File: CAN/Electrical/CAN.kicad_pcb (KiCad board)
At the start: 4 copper layers, 26 x 30 mm, 31 parts, among them J1 Conn_01x04, P1 USB_C_Plug_USB2.0, Q1 BSS214NW, Q2 BSS214NW, SW1 SW_Push, SW2 SW_DIP_x02, U1 ESP32-C3-MINI-1, U2 AP2112K-3.3, U3 SN65HVD230

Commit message: Updated project
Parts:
- TP5: value TestPoint -> VBUS
- TP6: value TestPoint -> 3.3V
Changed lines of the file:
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@@
     (property "ki_keywords" "switch normally-open pushbutton push-button")
     (attr smd)
-    (fp_text reference "SW1" (at 0 -0.254) (layer "F.SilkS")
+    (fp_text reference "SW1" (at -0.508 0) (layer "F.SilkS")
         (effects (font (size 0.5 0.5) (thickness 0.1) bold))
     )
@@
         (effects (font (size 0.8 0.8) (thickness 0.125)) (justify mirror))
     )
-    (fp_text value "TestPoint" (at -2.794 -0.508) (layer "B.SilkS")
+    (fp_text value "3.3V" (at -2.794 -0.508) (layer "B.SilkS")
         (effects (font (size 0.8 0.8) (thickness 0.125)) (justify mirror))
     )
@@
         (effects (font (size 0.8 0.8) (thickness 0.125)) (justify mirror))
     )
-    (fp_text value "TestPoint" (at -3.048 -0.508) (layer "B.SilkS")
+    (fp_text value "VBUS" (at -3.048 -0.508) (layer "B.SilkS")
         (effects (font (size 0.8 0.8) (thickness 0.125)) (justify mirror))
     )
@@
   (segment (start 71.46 89.254) (end 71.81 89.254) (width 0.125) (layer "F.Cu") (net 1))
   (segment (start 76.53 95.649) (end 76.53 99.599) (width 0.125) (layer "F.Cu") (net 1))
+  (segment (start 87.2451 95.504) (end 87.2451 93.4974) (width 0.125) (layer "F.Cu") (net 1))
   (segment (start 66.724 115.316) (end 68.9676 115.316) (width 0.125) (layer "F.Cu") (net 1))
   (segment (start 64.516 89.4936) (end 67.2089 92.1865) (width 0.125) (layer "F.Cu") (net 1))
@@
   (segment (start 71.49675 116.1985) (end 72.8275 114.86775) (width 0.125) (layer "F.Cu") (net 1))
   (segment (start 68.9676 115.316) (end 68.9676 113.0936) (width 0.125) (layer "F.Cu") (net 1))
+  (segment (start 87.2451 93.4974) (end 87.2705 93.472) (width 0.125) (layer "F.Cu") (net 1))
   (segment (start 70.58 102.164) (end 70.58 102.574) (width 0.125) (layer "F.Cu") (net 1))
   (segment (start 77.98 88.414) (end 77.98 88.679) (width 0.125) (layer "F.Cu") (net 1))
   (segment (start 66.675 93.135637) (end 67.624137 92.1865) (width 0.125) (layer "F.Cu") (net 1))
   (segment (start 82.22 88.664) (end 82.22 92.414) (width 0.125) (layer "F.Cu") (net 1))
+  (segment (start 87.2451 97.536) (end 87.2451 95.504) (width 0.125) (layer "F.Cu") (net 1))
   (segment (start 82.48 102.574) (end 82.48 105.49) (width 0.125) (layer "F.Cu") (net 1))
   (segment (start 79.793 108.177) (end 81.77 106.2) (width 0.125) (layer "F.Cu") (net 1))
@@
   (segment (start 70.63 94.424) (end 70.63 92.724) (width 0.125) (layer "F.Cu") (net 1))
   (segment (start 69.58 87.374) (end 71.46 89.254) (width 0.125) (layer "F.Cu") (net 1))
-  (segment (start 87.2451 97.536) (end 87.2451 91.4654) (width 0.125) (layer "F.Cu") (net 1))
   (segment (start 72.8275 110.906982) (end 75.557482 108.177) (width 0.125) (layer "F.Cu") (net 1))
   (segment (start 68.9676 115.316) (end 69.8501 116.1985) (width 0.125) (layer "F.Cu") (net 1))
@@
   (segment (start 87.2451 91.4654) (end 87.2705 91.44) (width 0.125) (layer "F.Cu") (net 1))
   (segment (start 68.796 112.922) (end 68.796 110.032) (width 0.125) (layer "F.Cu") (net 1))
+  (segment (start 87.2705 93.472) (end 87.2705 91.44) (width 0.125) (layer "F.Cu") (net 1))
   (segment (start 71.68 92.674) (end 71.73 92.724) (width 0.125) (layer "F.Cu") (net 1))
   (segment (start 78.505 99.599) (end 78.505 95.649) (width 0.125) (layer "F.Cu") (net 1))
@@
   (segment (start 83.82 87.39) (end 83.82 89.318518) (width 0.125) (layer "B.Cu") (net 2))
   (segment (start 83.82 102.186998) (end 84.836575 102.186998) (width 0.125) (layer "B.Cu") (net 2))
-  (segment (start 86.369417 86.7275) (end 84.738 86.7275) (width 0.125) (layer "B.Cu") (net 2))
   (segment (start 68.1629 91.2605) (end 66.8274 89.925) (width 0.125) (layer "B.Cu") (net 2))
-  (segment (start 83.82 102.186998) (end 85.813002 102.186998) (width 0.125) (layer "B.Cu") (net 2))
-  (segment (start 84.0755 87.39) (end 83.82 87.39) (width 0.125) (layer "B.Cu") (net 2))
-  (segment (start 84.738 86.7275) (end 84.0755 87.39) (width 0.125) (layer "B.Cu") (net 2))
+  (segment (start 86.369417 86.7275) (end 84.4825 86.7275) (width 0.125) (layer "B.Cu") (net 2))
+  (segment (start 86.6775 87.035583) (end 86.369417 86.7275) (width 0.125) (layer "B.Cu") (net 2))
   (segment (start 71.803002 102.186998) (end 83.82 102.186998) (width 0.125) (layer "B.Cu") (net 2))
   (segment (start 87.8965 113.7795) (end 86.614 115.062) (width 0.125) (layer "B.Cu") (net 2))
   (segment (start 83.82 89.318518) (end 81.878018 91.2605) (width 0.125) (layer "B.Cu") (net 2))
+  (segment (start 83.82 102.186998) (end 85.813002 102.186998) (width 0.125) (layer "B.Cu") (net 2))
+  (segment (start 86.6775 87.63128) (end 86.6775 87.035583) (width 0.125) (layer "B.Cu") (net 2))
   (segment (start 64.262 109.728) (end 71.803002 102.186998) (width 0.125) (layer "B.Cu") (net 2))
-  (segment (start 86.7575 101.2425) (end 86.7575 87.115583) (width 0.125) (layer "B.Cu") (net 2))
   (segment (start 81.878018 91.2605) (end 68.1629 91.2605) (width 0.125) (layer "B.Cu") (net 2))
   (segment (start 64.262 110.998) (end 64.262 109.728) (width 0.125) (layer "B.Cu") (net 2))
   (segment (start 84.836575 102.186998) (end 87.8965 105.246923) (width 0.125) (layer "B.Cu") (net 2))
+  (segment (start 86.106 88.20278) (end 86.6775 87.63128) (width 0.125) (layer "B.Cu") (net 2))
   (segment (start 87.8965 105.246923) (end 87.8965 113.7795) (width 0.125) (layer "B.Cu") (net 2))
-  (segment (start 85.813002 102.186998) (end 86.7575 101.2425) (width 0.125) (layer "B.Cu") (net 2))
-  (segment (start 86.7575 87.115583) (end 86.369417 86.7275) (width 0.125) (layer "B.Cu") (net 2))
+  (segment (start 85.813002 102.186998) (end 86.106 101.894) (width 0.125) (layer "B.Cu") (net 2))
+  (segment (start 84.4825 86.7275) (end 83.82 87.39) (width 0.125) (layer "B.Cu") (net 2))
+  (segment (start 86.106 101.894) (end 86.106 88.20278) (width 0.125) (layer "B.Cu") (net 2))
   (segment (start 70.559 90.043) (end 73.476 90.043) (width 0.125) (layer "F.Cu") (net 3))
   (segment (start 73.476 90.043) (end 74.48 89.039) (width 0.125) (layer "F.Cu") (net 3))
@@
   (segment (start 70.7992 107.5944) (end 75.2956 107.5944) (width 0.125) (layer "F.Cu") (net 15))
   (segment (start 70.812 109.366) (end 70.812 107.6072) (width 0.125) (layer "F.Cu") (net 15))
+  (segment (start 85.09 99.584) (end 85.09 97.6161) (width 0.125) (layer "F.Cu") (net 16))
   (segment (start 86.94 90.3385) (end 86.233 91.0455) (width 0.125) (layer "F.Cu") (net 16))
   (segment (start 85.1955 93.472) (end 86.233 92.4345) (width 0.125) (layer "F.Cu") (net 16))
+  (segment (start 85.1701 93.4974) (end 85.1955 93.472) (width 0.125) (layer "F.Cu") (net 16))
   (segment (start 86.233 92.4345) (end 86.233 91.0455) (width 0.125) (layer "F.Cu") (net 16))
   (segment (start 86.94 88.235) (end 86.94 90.3385) (width 0.125) (layer "F.Cu") (net 16))
-  (segment (start 85.1955 93.472) (end 85.1955 99.4785) (width 0.125) (layer "F.Cu") (net 16))
   (segment (start 85.1955 99.4785) (end 85.09 99.584) (width 0.125) (layer "F.Cu") (net 16))
+  (segment (start 85.1701 95.504) (end 85.1701 93.4974) (width 0.125) (layer "F.Cu") (net 16))
   (segment (start 86.095 87.39) (end 86.94 88.235) (width 0.125) (layer "F.Cu") (net 16))
+  (segment (start 85.1701 97.536) (end 85.1701 95.504) (width 0.125) (layer "F.Cu") (net 16))
   (segment (start 71.856 95.224) (end 70.63 95.224) (width 0.125) (layer "F.Cu") (net 16))
   (segment (start 72.35911 95.72711) (end 71.856 95.224) (width 0.125) (layer "F.Cu") (net 16))
+  (segment (start 85.09 97.6161) (end 85.1701 97.536) (width 0.125) (layer "F.Cu") (net 16))
   (segment (start 72.35911 97.75911) (end 72.35911 95.72711) (width 0.125) (layer "F.Cu") (net 16))
   (via (at 65.405 93.424) (size 0.8) (drill 0.4) (layers "F.Cu" "B.Cu") (net 16))

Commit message: Updated board
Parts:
- removed Q1, Q2: BSS214NW, Package_TO_SOT_SMD:SOT-323_SC-70
- removed the R4 at (69.8, 107.6)
- removed SW2: SW_DIP_x02, Button_Switch_SMD:SW_DIP_SPSTx02_Slide_Copal_CHS-02A_W5.08mm_P1.27mm_JPin
- added D2: LED, LED_SMD:LED_0805_2012Metric_Pad1.15x1.40mm_HandSolder, F.Cu at (63.2, 114.2)
- added R3: 5.1k, Resistor_SMD:R_0805_2012Metric_Pad1.20x1.40mm_HandSolder, B.Cu at (64.4, 91.9)
- added R6: 10k, Resistor_SMD:R_0805_2012Metric_Pad1.20x1.40mm_HandSolder, F.Cu at (85.3, 110.1)
- added R7: 120R, Resistor_SMD:R_0805_2012Metric_Pad1.20x1.40mm_HandSolder, F.Cu at (65.5, 101.5)
- added U5: FODM217D, Package_SO:SOP-4_4.4x2.6mm_P1.27mm, F.Cu at (67.6, 112.0)
- D1: value D -> D_Schottky
- J1: value Conn_01x04 -> Conn_01x05; footprint Connector_PinSocket_2.54mm:PinSocket_1x04_P2.54mm_Horizontal -> Connector_PinSocket_2.54mm:PinSocket_1x05_P2.54mm_Horizontal
- R5: value 60R -> 5.1k
- SW1: value SW_Push -> Reset
- moved SW1 21.3 mm to (85.9, 114.8)
- moved C5 20.8 mm to (85.3, 112.1), turned to 0 degrees
- moved TP6 19.2 mm to (63.6, 95.6)
- moved TP8 18.0 mm to (81.2, 94.2)
- moved TP7 18.0 mm to (78.5, 94.2)
- moved TP5 12.7 mm to (63.6, 98.3)
- moved R5 8.36 mm to (63.2, 110.3), turned to -90 degrees
- moved J1 2.80 mm to (71.4, 106.2)
- moved R4 1.80 mm to (63.5, 101.5), turned to -90 degrees
- renumbered R3 to R4
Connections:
- J1 pad 1: Net-(J1-Pin_1) -> /GPIO6
- J1 pad 2: CAN_H -> VBUS
- J1 pad 3: CAN_L -> CAN_H
- J1 pad 4: GND -> CAN_L
- P1 pad B5: unconnected-(P1-VCONN-PadB5) -> Net-(P1-VCONN)
- R5 pad 1: CAN_L -> VBUS
- R5 pad 2: GND -> Net-(D2-A)
- U1 pad 20: unconnected-(U1-GPIO6-Pad20) -> /GPIO6
- U3 pad 8: unconnected-(U3-Rs-Pad8) -> Net-(U3-Rs)
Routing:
- net VBUS: track 89.3 -> 64.4 mm
- net Net-(U3-Rs): track 0.00 -> 24.4 mm, vias 0 -> 2
- net GND: track 148.4 -> 125.1 mm, vias 2 -> 4
- net +3.3V: track 71.8 -> 52.9 mm
- net Net-(R7-Pad2): track 0.00 -> 14.4 mm, vias 0 -> 2
- net Net-(J1-Pin_1): track 14.0 -> 0.00 mm, vias 1 -> 0
- net Net-(P1-VCONN): track 0.00 -> 13.7 mm, vias 0 -> 2
- net CAN_L: track 33.4 -> 21.3 mm
- net /TXD: track 18.1 -> 6.14 mm, vias 2 -> 1
- net CAN_H: track 19.2 -> 30.7 mm, vias 0 -> 1
- net /RXD: track 16.5 -> 5.08 mm, vias 2 -> 1
- net /GPIO6: track 0.00 -> 9.05 mm, vias 0 -> 1
- net /EN: track 37.5 -> 33.7 mm
- net Net-(D1-A): track 18.7 -> 20.7 mm, vias 2 -> 3
- net Net-(D2-A): track 0.00 -> 1.79 mm
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
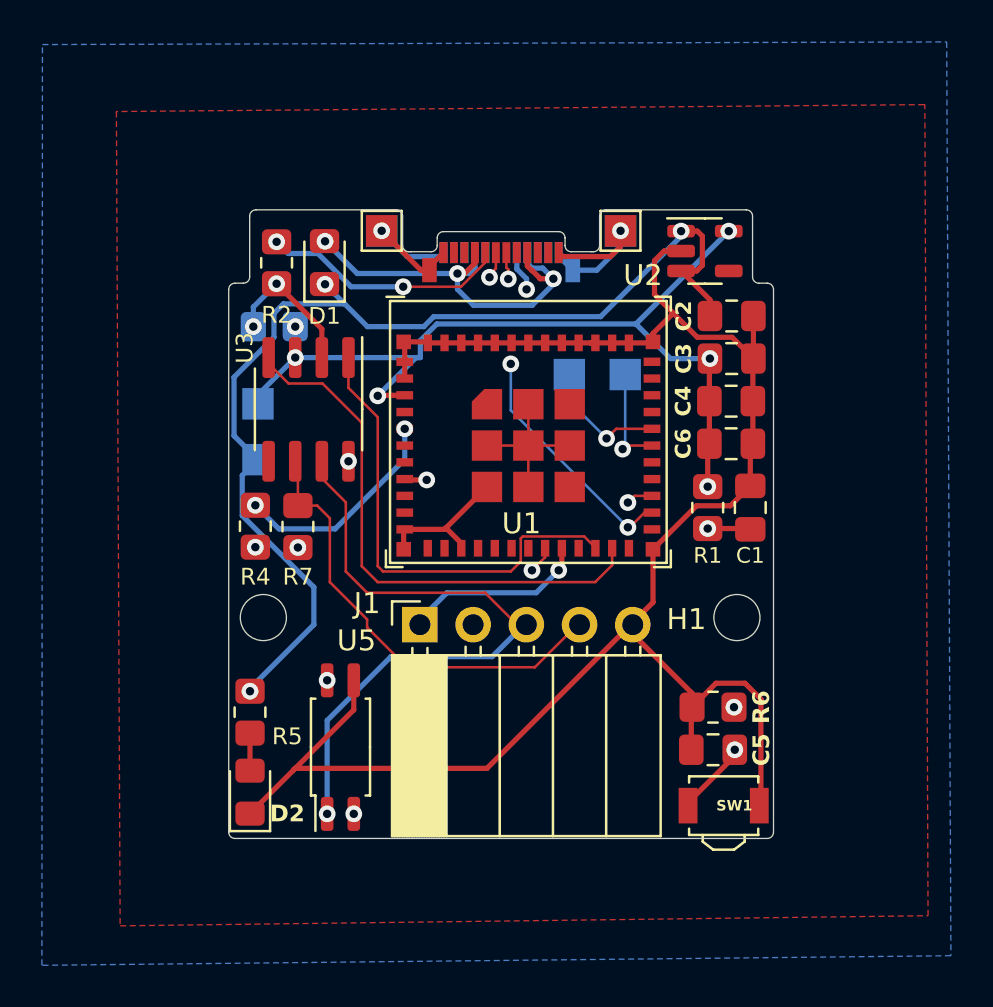
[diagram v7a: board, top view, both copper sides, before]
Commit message: Added Resistor to protect optocoppler diode
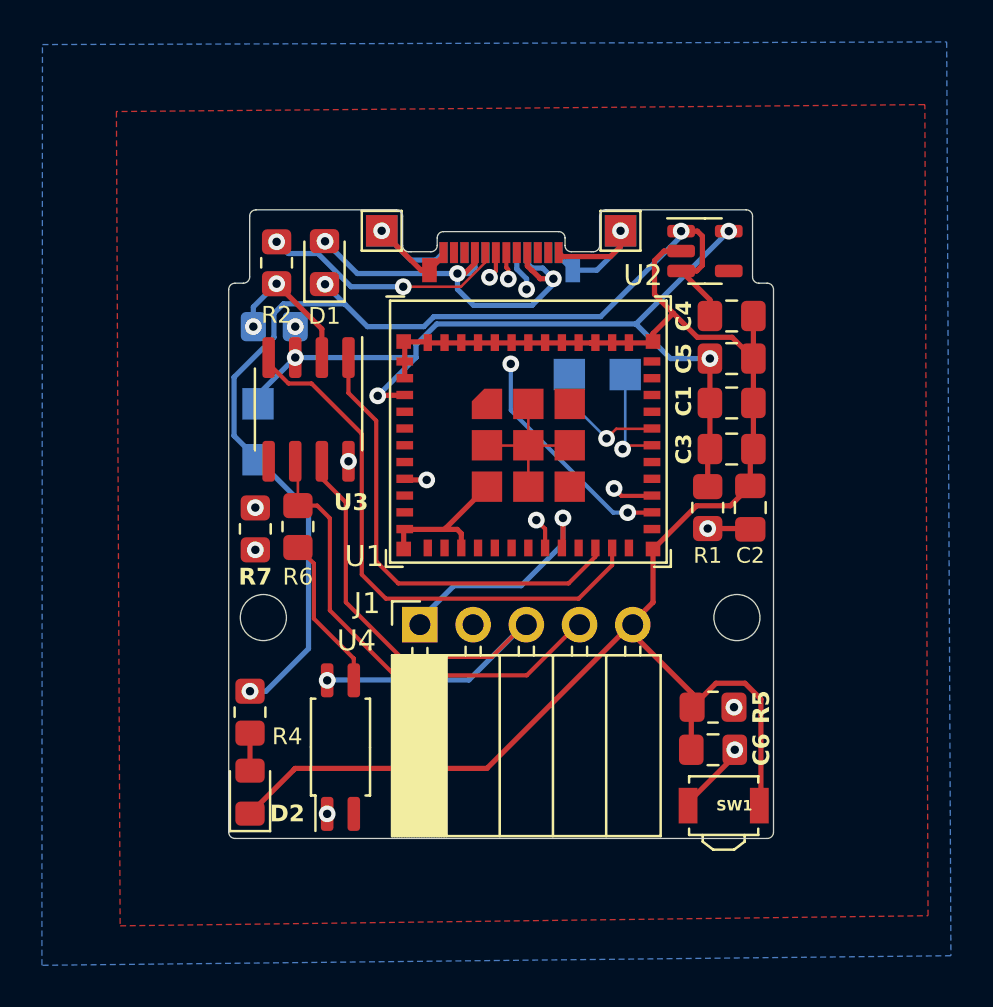
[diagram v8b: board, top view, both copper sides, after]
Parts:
- removed the C4 at (86.2, 95.5)
- removed the C6 at (86.2, 97.5)
- removed the R4 at (63.5, 101.5)
- added C1: 10uF, Capacitor_SMD:C_0805_2012Metric_Pad1.18x1.45mm_HandSolder, F.Cu at (86.2, 95.6)
- added C3: 0.1uF, Capacitor_SMD:C_0805_2012Metric_Pad1.18x1.45mm_HandSolder, F.Cu at (86.2, 97.8)
- added R7: 20R, Resistor_SMD:R_0805_2012Metric_Pad1.20x1.40mm_HandSolder, F.Cu at (63.5, 101.6)
- renumbered C1 to C2, C2 to C4, C3 to C5, C5 to C6, R5 to R4, R6 to R5, R7 to R6, U5 to U4
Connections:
- R6 pad 2: Net-(R7-Pad2) -> Net-(R6-Pad2)
- U1 pad 5: Net-(U1-GPIO2/ADC1_CH2) -> unconnected-(U1-GPIO2/ADC1_CH2-Pad5)
- U4 pad 1: CAN_H -> Net-(R7-Pad2)
- U4 pad 2: Net-(R7-Pad2) -> GND
- U4 pad 3: GND -> Net-(R6-Pad2)
- U4 pad 4: /TERM -> CAN_H
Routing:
- net +3.3V: track 52.9 -> 40.9 mm, vias 6 -> 4
- net Net-(U1-GPIO2/ADC1_CH2): track 10.4 -> 0.00 mm, vias 2 -> 0
- net Net-(R6-Pad2): track 0.00 -> 7.44 mm
- net GND: track 125.1 -> 120.2 mm
- net CAN_H: track 30.7 -> 27.5 mm
- net /GPIO6: track 9.05 -> 11.4 mm
- net Net-(R7-Pad2): track 14.4 -> 16.0 mm
- net /D+: track 17.9 -> 16.3 mm
- net /D-: track 17.7 -> 16.4 mm
- net /TERM: track 14.4 -> 15.5 mm
- net CAN_L: track 21.3 -> 22.2 mm
- net /EN: track 33.7 -> 33.0 mm
- net /CAN_RX: track 26.2 -> 26.7 mm
- net /CAN_TX: track 22.6 -> 22.1 mm
- added copper zone on B.Cu, net VBUS
- removed copper zone on B.Cu, net +3.3V
